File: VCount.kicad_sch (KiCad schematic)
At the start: 10 parts, among them SW201 SW_DIP_x10, U202 GAL22V10, U203 74HCT163, U204 74HCT163, U205 74HCT163

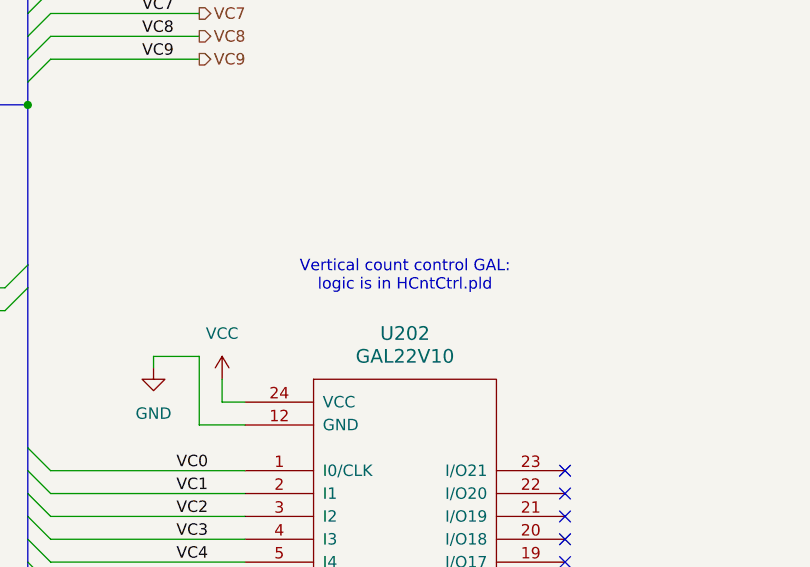
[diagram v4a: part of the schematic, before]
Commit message: use 74ACT parts where needed (e.g., HCount)
Also, I don't think the 74HCT365 buffer is needed for
the output DAC. I think a single intensity output can
feed into all three color outputs. It's a voltage source,
so it shouldn't really matter what load is on it.
(Need to test this out in simulation.)
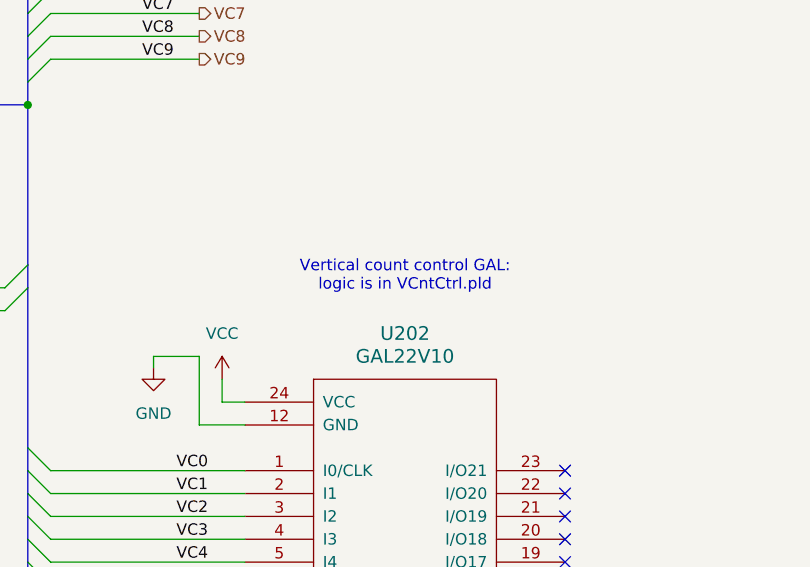
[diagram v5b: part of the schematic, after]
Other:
- note added: "Vertical count control GAL: logic is in VCntCtrl.pld"
- note removed: "Vertical count control GAL: logic is in HCntCtrl.pld"
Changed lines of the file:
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@@
 		)
 	)
-	(text "Vertical count control GAL:\nlogic is in HCntCtrl.pld"
+	(text "Vertical count control GAL:\nlogic is in VCntCtrl.pld"
 		(exclude_from_sim no)
 		(at 220.98 68.58 0)

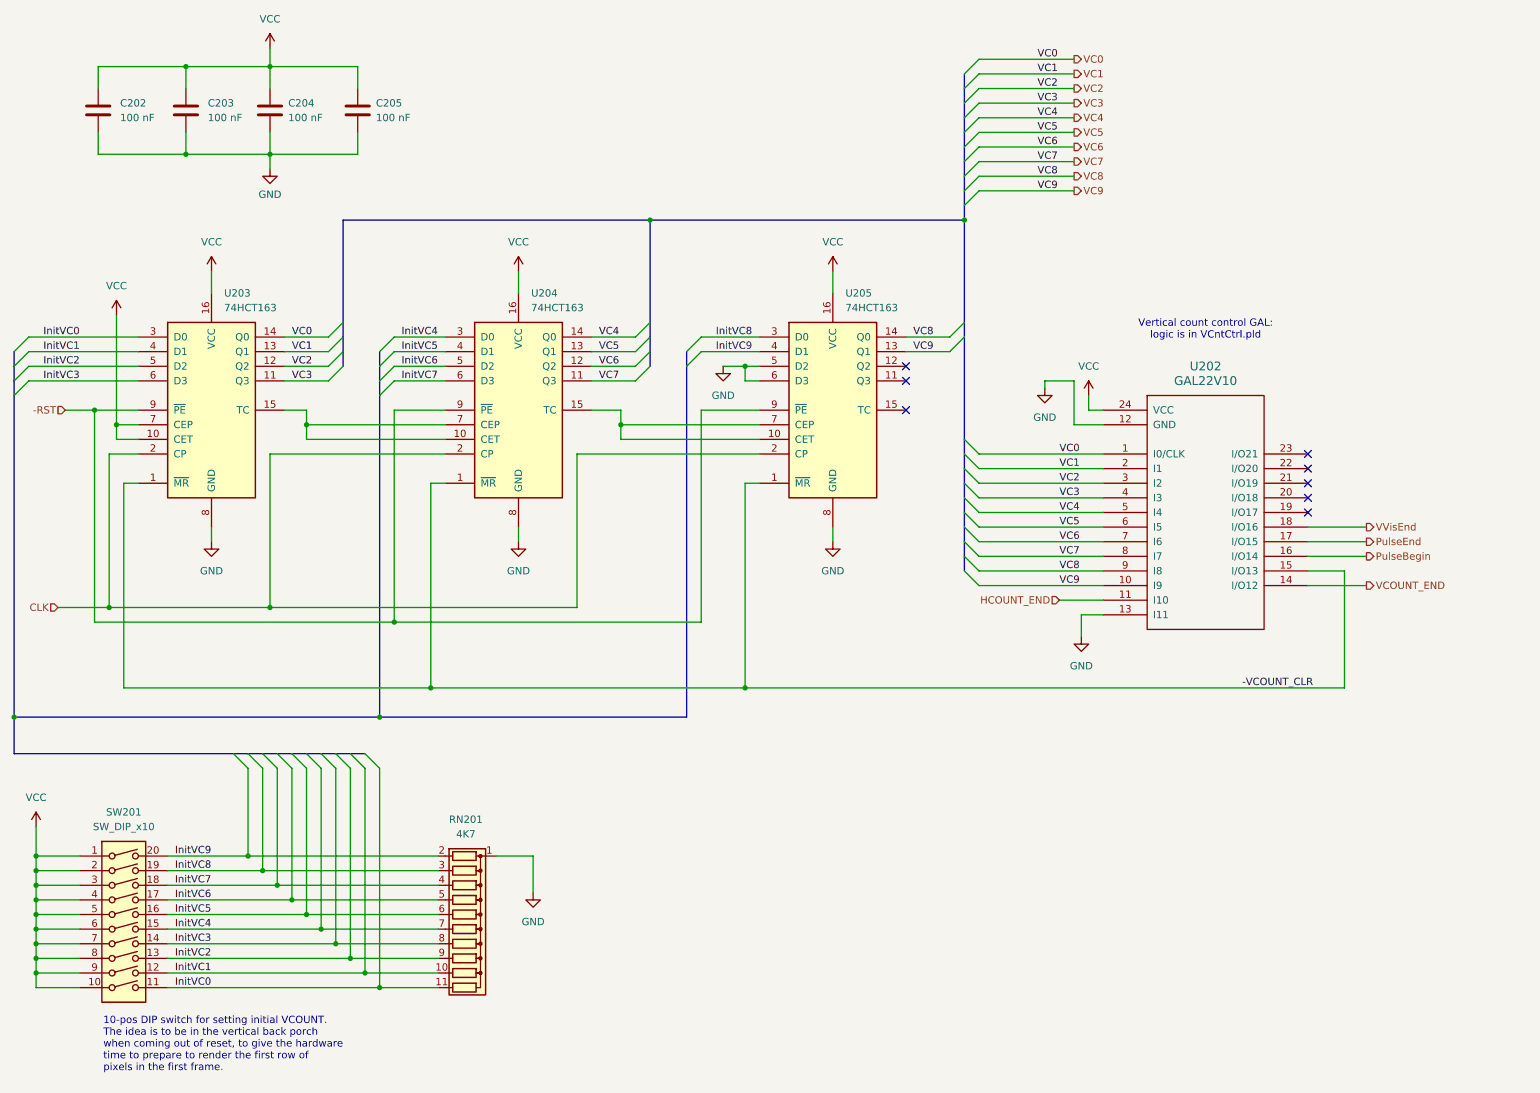
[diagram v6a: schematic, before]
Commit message: incr VCOUNT only when HCOUNT_END asserted
As the schematic was drawn originally (and as the
prototype VCount module was wired originally),
VCOUNT was incremented on every clock, which
obviously isn't right.

Some other misc. cleanups such as specifying
74ACT163 rather than 74HCT163 for the counters.
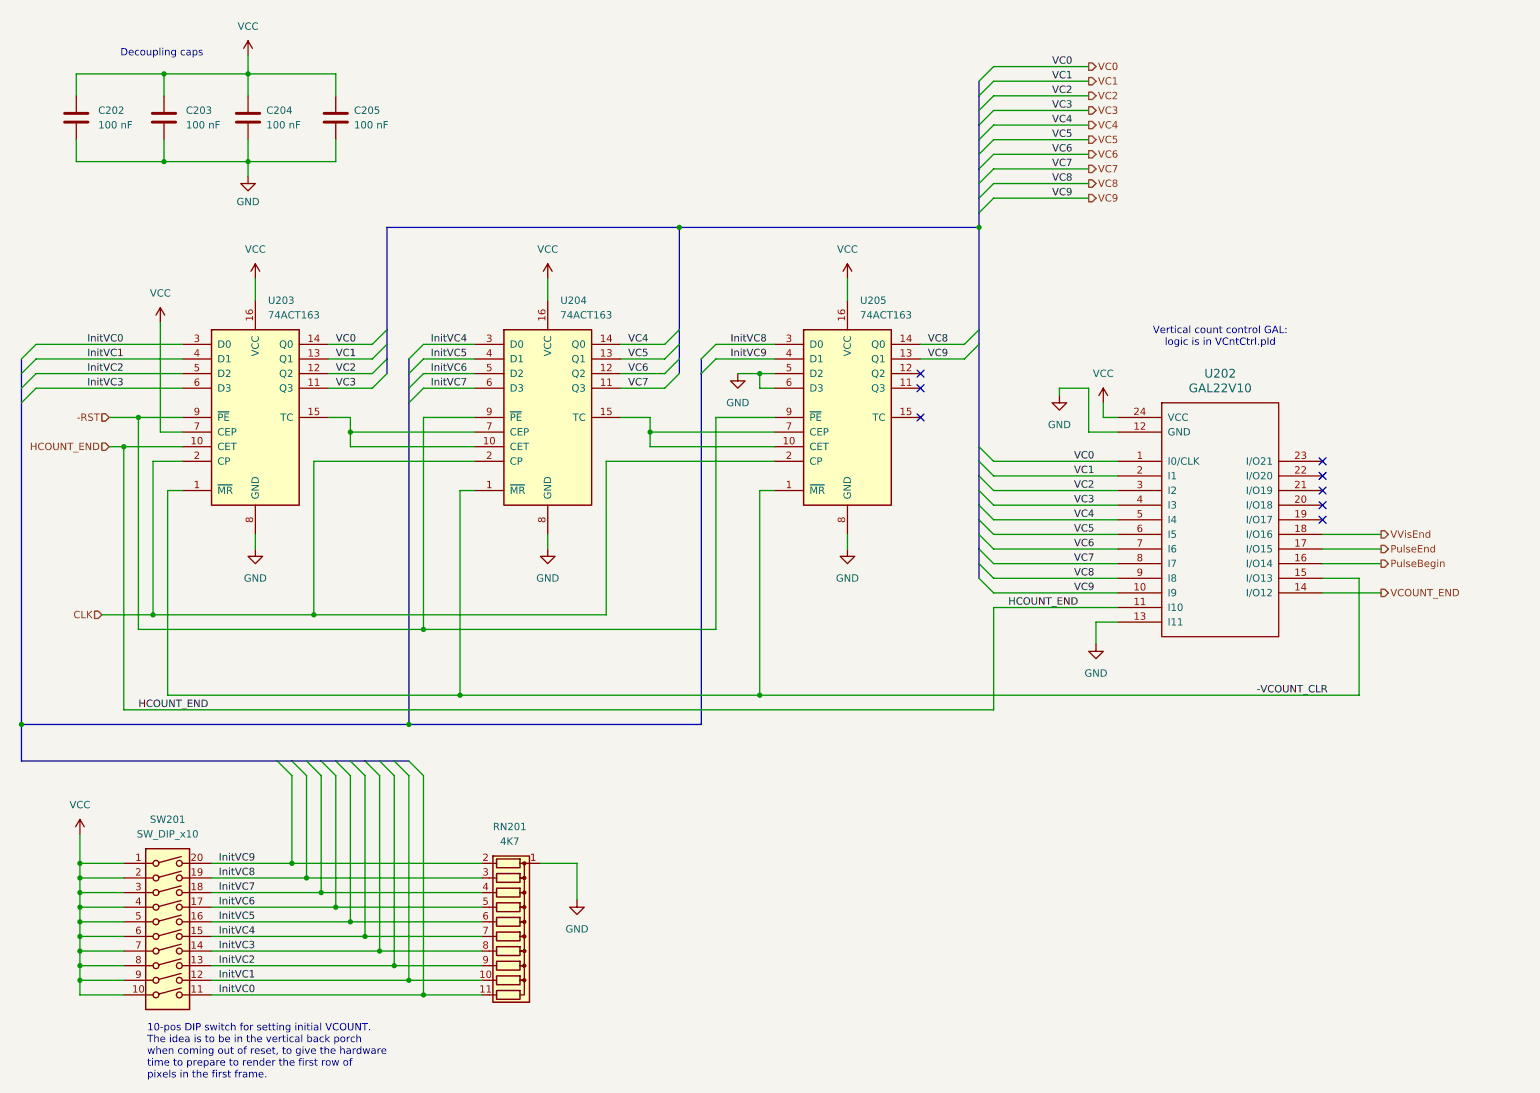
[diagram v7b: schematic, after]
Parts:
- U203, U204, U205: value 74HCT163 -> 74ACT163
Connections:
- net HCOUNT_END: now also U203.10 (CET)
- net VCC: no longer U203.10 (CET)
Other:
- note added: "Decoupling caps"
- moved on the sheet: C202, C203, C204, C205, RN201, SW201, U202, U203, U204, U205
